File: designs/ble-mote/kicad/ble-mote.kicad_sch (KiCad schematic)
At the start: 37 parts, among them J1 TYPE-C-31-M-12, Q1 PMBT3904,235, Q2 PMBT3904,235, U1 TPD3S014DBVR, U2 AP2112K-3.3TRG1, U3 CP2105-F01-GM, U4 HDC1080DMBR, U6 FM-B2020RGBA-HG

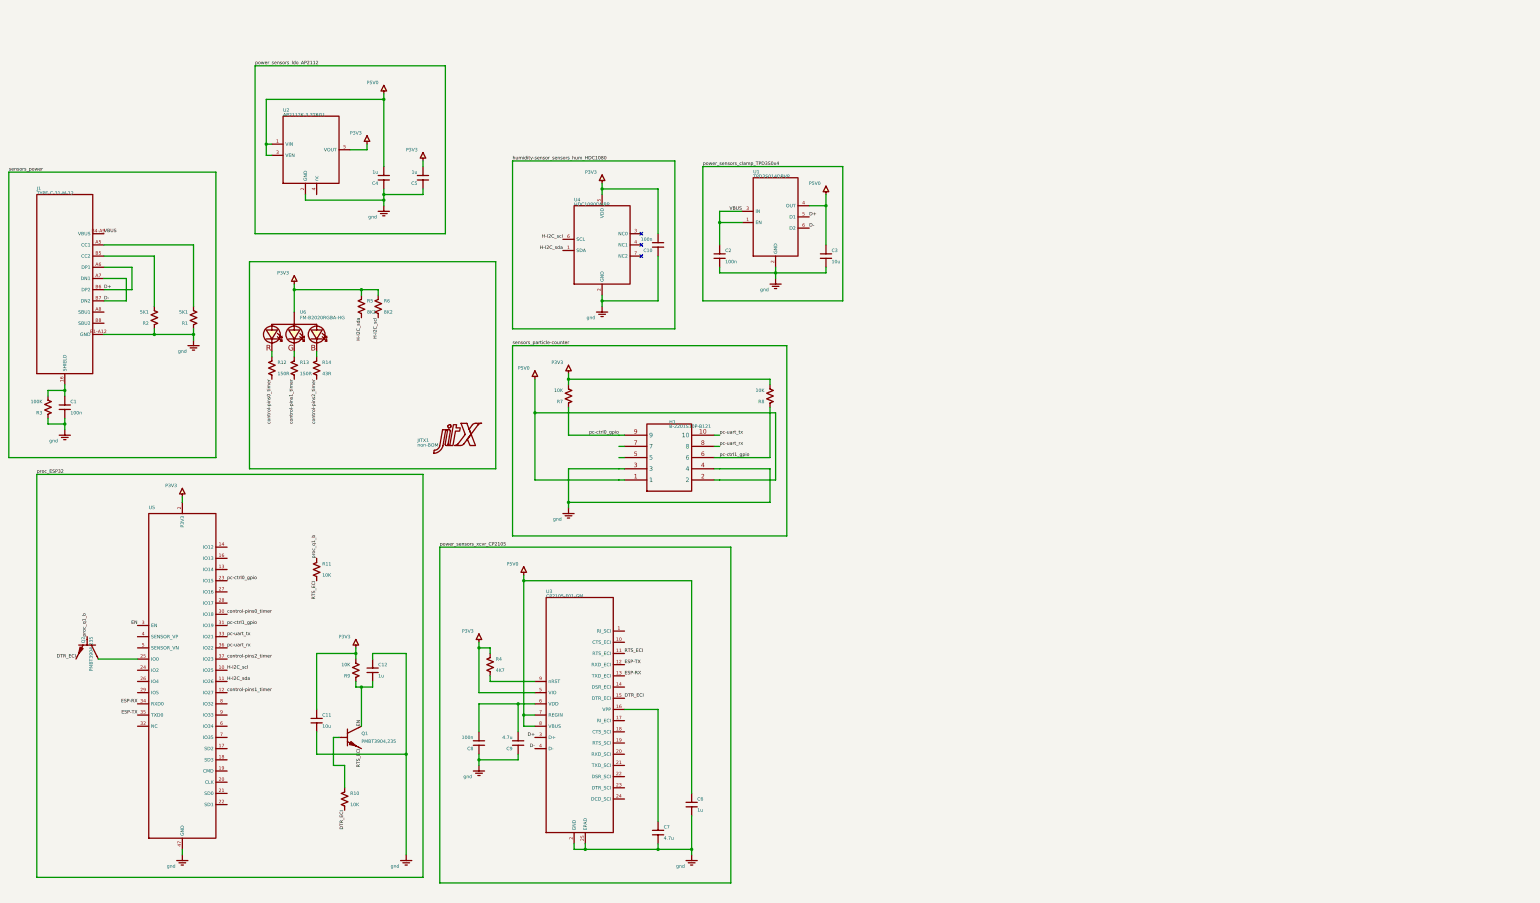
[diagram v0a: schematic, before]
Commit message: Schematic export issue in kicad
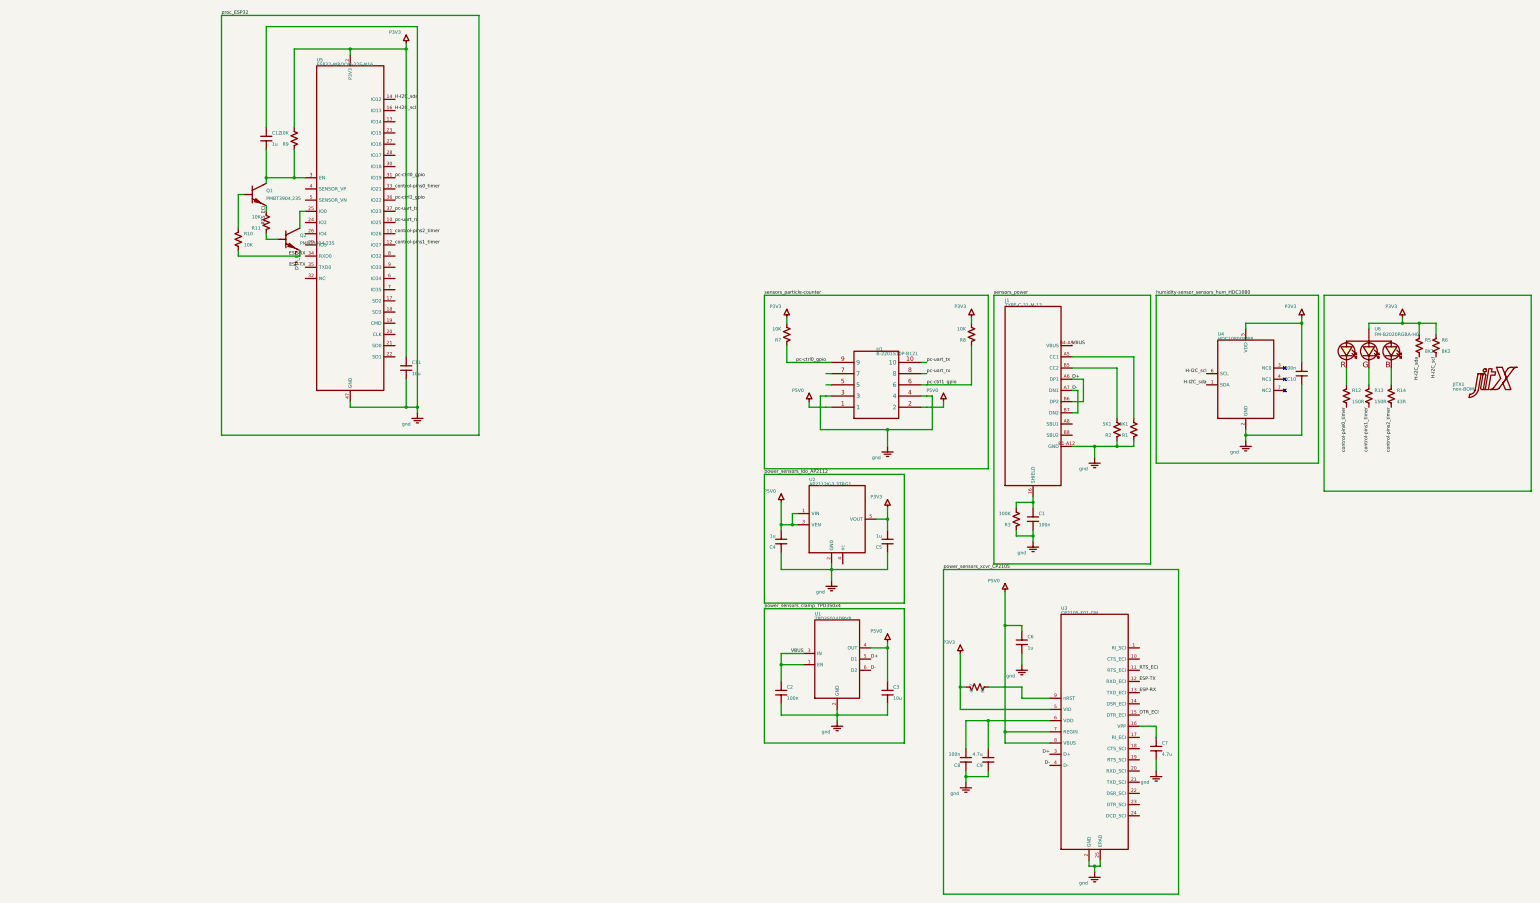
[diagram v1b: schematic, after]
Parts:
- removed R1: 5K1, ble-mote:Pkg0402_4, symbol my_resistor_1
- removed R10: 10K, ble-mote:Pkg0402_4, symbol my_resistor_8
- removed R11: 10K, ble-mote:Pkg0402_4, symbol my_resistor_11
- removed R12: 150R, ble-mote:Pkg0402_4, symbol my_resistor
- removed R13: 150R, ble-mote:Pkg0402_4, symbol my_resistor_3
- removed R14: 43R, ble-mote:Pkg0402_4, symbol my_resistor_5
- removed R2: 5K1, ble-mote:Pkg0402_4, symbol my_resistor_6
- removed R3: 100K, ble-mote:Pkg0402_4, symbol my_resistor_10
- removed R4: 4K7, ble-mote:Pkg0402_4, symbol my_resistor_9
- removed R5, R6: 8K2, ble-mote:Pkg0402, symbol my_resistor_7
- removed R7: 10K, ble-mote:Pkg0402_4, symbol my_resistor_12
- removed R8: 10K, ble-mote:Pkg0402_4, symbol my_resistor_2
- removed R9: 10K, ble-mote:Pkg0402_4, symbol my_resistor_4
- added R1: 5K1, ble-mote:Pkg0402_4, symbol my_resistor_3
- added R10: 10K, ble-mote:Pkg0402_4, symbol my_resistor_10
- added R11: 10K, ble-mote:Pkg0402_4, symbol my_resistor
- added R12: 150R, ble-mote:Pkg0402_4, symbol my_resistor_2
- added R13: 150R, ble-mote:Pkg0402_4, symbol my_resistor_5
- added R14: 43R, ble-mote:Pkg0402_4, symbol my_resistor_7
- added R2: 5K1, ble-mote:Pkg0402_4, symbol my_resistor_8
- added R3: 100K, ble-mote:Pkg0402_4, symbol my_resistor_12
- added R4: 4K7, ble-mote:Pkg0402_4, symbol my_resistor_11
- added R5, R6: 8K2, ble-mote:Pkg0402, symbol my_resistor_9
- added R7: 10K, ble-mote:Pkg0402_4, symbol my_resistor_1
- added R8: 10K, ble-mote:Pkg0402_4, symbol my_resistor_4
- added R9: 10K, ble-mote:Pkg0402_4, symbol my_resistor_6
- U5: value (none) -> ESP32-WROOM-32E-N16; MPN (none) -> ESP32-WROOM-32E-N16
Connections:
- net DTR_ECI: now also R10.1
- net H-I2C_scl: now also U5.16 (IO13), R6.1; no longer U5.10 (IO25)
- net H-I2C_sda: now also U5.14 (IO12), R5.1; no longer U5.11 (IO26)
- net RTS_ECI: now also R11.1
- net control-pins0_timer: now also U5.33 (IO21), R12.1; no longer U5.30 (IO18)
- net control-pins1_timer: now also R13.1
- net control-pins2_timer: now also U5.11 (IO26), R14.1; no longer U5.37 (IO23)
- net pc-ctrl0_gpio: now also U5.31 (IO19), R7.2; no longer U5.23 (IO15)
- net pc-ctrl1_gpio: now also U5.36 (IO22), R8.2; no longer U5.31 (IO19)
- net pc-uart_rx: now also U5.10 (IO25); no longer U5.36 (IO22)
- net pc-uart_tx: now also U5.37 (IO23); no longer U5.33 (IO21)
- net at C1.1, J1.13 (SHIELD), J1.14 (SHIELD)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: now also R3.1
- net at C1.2: now also R3.2
- net at C11.2, C12.1: now also U5.1 (GND), U5.15 (GND), U5.38 (GND), U5.39 (GND), U5.40 (GND), U5.41 (GND), U5.42 (GND), U5.43 (GND), U5.44 (GND), U5.45 (GND), U5.46 (GND), U5.47 (GND)
- net at U6.4 (l_a): now also R5.2, R6.2
- net at C11.1: now also U5.2 (P3V3), R9.1
- net at U2.5 (VOUT): now also C5.2
- net at U3.2 (GND), U3.25 (EPAD): no longer C6.2, C7.2
- net at U3.5 (VIO): now also R4.2
- net at U3.9 (nRST): now also R4.1
- net at H1.1: no longer H1.2
- net at J1.A1-B12 (GND), J1.B1-A12 (GND): now also R1.2, R2.2
- net at J1.A5 (CC1): now also R1.1
- net at J1.B5 (CC2): now also R2.1
- net at Q1.1 (b): now also R10.2
- net at U6.1 (l_r): now also R12.2
- net at U6.2 (l_b): now also R14.2
- net at U6.3 (l_g): now also R13.2
- net EN: no longer names the net of C12.2, Q1.3 (c), U5.3 (EN)
- net EN: now also R9.2
- net proc_q1_b: no longer names the net of Q2.1 (b)
- net proc_q1_b: now also R11.2
